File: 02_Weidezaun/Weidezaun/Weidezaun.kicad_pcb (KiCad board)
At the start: 2 copper layers, 34.3 x 47.7 mm, 8 parts, among them J1 Screw_Terminal_01x02, J2 Screw_Terminal_01x02, Q1 2N7000

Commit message: review
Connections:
- J1 pad 2: Net-(BZ1-Pad1) -> +9V
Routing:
- net +9V: track 29.3 -> 69.9 mm
- net Net-(BZ1-Pad1): track 32.9 -> 18.7 mm
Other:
- board text added: "GND"
- board text added: "SPEAKER"
- board text added: "VCC"
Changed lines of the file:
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@@
   (general
     (thickness 1.6)
-    (drawings 4)
-    (tracks 16)
+    (drawings 7)
+    (tracks 20)
     (zones 0)
     (modules 8)
@@
     (47 F.CrtYd user)
     (48 B.Fab user)
-    (49 F.Fab user)
+    (49 F.Fab user hide)
   )
   (setup
@@
     (pad_to_mask_clearance 0)
     (aux_axis_origin 0 0)
-    (visible_elements FFFFFF7F)
+    (visible_elements 7FFFFFFF)
     (pcbplotparams
       (layerselection 0x010fc_ffffffff)
@@
     (descr "simple 2-pin terminal block, pitch 5.08mm, revamped version of bornier2")
     (tags "terminal block bornier2")
-    (fp_text reference J1 (at 2.73 -2.88) (layer F.SilkS)
+    (fp_text reference J1 (at -0.756 -2.9304) (layer F.SilkS)
       (effects (font (size 1 1) (thickness 0.15)))
     )
     (fp_text value Screw_Terminal_01x02 (at 2.54 5.08) (layer F.Fab)
-      (effects (font (size 1 1) (thickness 0.15)))
-    )
-    (fp_text user %R (at 2.54 0) (layer F.Fab)
       (effects (font (size 1 1) (thickness 0.15)))
     )
@@
     (fp_line (start 7.79 4) (end 7.79 -4) (layer F.CrtYd) (width 0.05))
     (fp_line (start 7.79 4) (end -2.71 4) (layer F.CrtYd) (width 0.05))
+    (fp_text user %R (at 2.54 0) (layer F.Fab)
+      (effects (font (size 1 1) (thickness 0.15)))
+    )
     (pad 2 thru_hole circle (at 5.08 0) (size 3 3) (drill 1.52) (layers *.Cu *.Mask)
-      (net 2 "Net-(BZ1-Pad1)"))
+      (net 3 +9V))
     (pad 1 thru_hole rect (at 0 0) (size 3 3) (drill 1.52) (layers *.Cu *.Mask)
       (net 1 "Net-(BZ1-Pad2)"))
@@
   (module custom:testpoint_15x15 (layer F.Cu)
     (at 120.37 101.815001)
-    (fp_text reference TP2 (at 0 -8.265001) (layer F.SilkS)
+    (fp_text reference TP2 (at 5.8934 -6.615801) (layer Dwgs.User)
       (effects (font (size 1 1) (thickness 0.15)))
     )
@@
   (module custom:testpoint_15x15 (layer F.Cu)
     (at 120.37 71.264999)
-    (fp_text reference TP1 (at 0 8.355001) (layer F.SilkS)
+    (fp_text reference TP1 (at 0 8.355001) (layer Dwgs.User)
       (effects (font (size 1 1) (thickness 0.15)))
     )
@@
     (fp_text value 220R (at 3.81 1.92) (layer F.Fab)
       (effects (font (size 1 1) (thickness 0.15)))
-    )
-    (fp_text user %R (at 3.81 0) (layer F.Fab)
-      (effects (font (size 0.72 0.72) (thickness 0.108)))
     )
     (fp_line (start 2.01 -0.8) (end 2.01 0.8) (layer F.Fab) (width 0.1))
@@
     (fp_line (start 8.57 1.05) (end 8.57 -1.05) (layer F.CrtYd) (width 0.05))
     (fp_line (start 8.57 -1.05) (end -0.95 -1.05) (layer F.CrtYd) (width 0.05))
+    (fp_text user %R (at 3.81 0) (layer F.Fab)
+      (effects (font (size 0.72 0.72) (thickness 0.108)))
+    )
     (pad 2 thru_hole oval (at 7.62 0) (size 1.4 1.4) (drill 0.7) (layers *.Cu *.Mask)
       (net 2 "Net-(BZ1-Pad1)"))
@@
     (fp_text value 1M (at 3.81 1.92 90) (layer F.Fab)
       (effects (font (size 1 1) (thickness 0.15)))
-    )
-    (fp_text user %R (at 3.81 0 90) (layer F.Fab)
-      (effects (font (size 0.72 0.72) (thickness 0.108)))
     )
     (fp_line (start 2.01 -0.8) (end 2.01 0.8) (layer F.Fab) (width 0.1))
@@
     (fp_line (start 8.57 1.05) (end 8.57 -1.05) (layer F.CrtYd) (width 0.05))
     (fp_line (start 8.57 -1.05) (end -0.95 -1.05) (layer F.CrtYd) (width 0.05))
+    (fp_text user %R (at 3.81 0 90) (layer F.Fab)
+      (effects (font (size 0.72 0.72) (thickness 0.108)))
+    )
     (pad 2 thru_hole oval (at 7.62 0 90) (size 1.4 1.4) (drill 0.7) (layers *.Cu *.Mask)
       (net 4 GND))
@@
       (effects (font (size 1 1) (thickness 0.15)))
     )
-    (fp_arc (start 1.27 0) (end 1.27 -2.6) (angle 135) (layer F.SilkS) (width 0.12))
-    (fp_arc (start 1.27 0) (end 1.27 -2.48) (angle -135) (layer F.Fab) (width 0.1))
-    (fp_arc (start 1.27 0) (end 1.27 -2.6) (angle -135) (layer F.SilkS) (width 0.12))
-    (fp_arc (start 1.27 0) (end 1.27 -2.48) (angle 135) (layer F.Fab) (width 0.1))
-    (fp_text user %R (at 1.27 0 90) (layer F.Fab)
-      (effects (font (size 1 1) (thickness 0.15)))
-    )
     (fp_line (start -0.53 1.85) (end 3.07 1.85) (layer F.SilkS) (width 0.12))
     (fp_line (start -0.5 1.75) (end 3 1.75) (layer F.Fab) (width 0.1))
@@
     (fp_line (start 4 2.01) (end 4 -2.73) (layer F.CrtYd) (width 0.05))
     (fp_line (start 4 2.01) (end -1.46 2.01) (layer F.CrtYd) (width 0.05))
+    (fp_arc (start 1.27 0) (end 1.27 -2.6) (angle 135) (layer F.SilkS) (width 0.12))
+    (fp_arc (start 1.27 0) (end 1.27 -2.48) (angle -135) (layer F.Fab) (width 0.1))
+    (fp_arc (start 1.27 0) (end 1.27 -2.6) (angle -135) (layer F.SilkS) (width 0.12))
+    (fp_arc (start 1.27 0) (end 1.27 -2.48) (angle 135) (layer F.Fab) (width 0.1))
+    (fp_text user %R (at 1.27 0 90) (layer F.Fab)
+      (effects (font (size 1 1) (thickness 0.15)))
+    )
     (pad 1 thru_hole rect (at 0 0 270) (size 1.05 1.5) (drill 0.75) (layers *.Cu *.Mask)
       (net 4 GND))
@@
     )
     (fp_text value Screw_Terminal_01x02 (at 2.54 5.08) (layer F.Fab)
-      (effects (font (size 1 1) (thickness 0.15)))
-    )
-    (fp_text user %R (at 2.54 0) (layer F.Fab)
       (effects (font (size 1 1) (thickness 0.15)))
     )
@@
     (fp_line (start 7.79 4) (end 7.79 -4) (layer F.CrtYd) (width 0.05))
     (fp_line (start 7.79 4) (end -2.71 4) (layer F.CrtYd) (width 0.05))
+    (fp_text user %R (at 2.54 0) (layer F.Fab)
+      (effects (font (size 1 1) (thickness 0.15)))
+    )
     (pad 2 thru_hole circle (at 5.08 0 180) (size 3 3) (drill 1.52) (layers *.Cu *.Mask)
       (net 3 +9V))
@@
       (effects (font (size 1 1) (thickness 0.15)))
     )
-    (fp_arc (start 2.5 0) (end -3.9 -1.5) (angle -26.38121493) (layer F.SilkS) (width 0.12))
-    (fp_text user %R (at 2.5 -2.43) (layer F.Fab)
-      (effects (font (size 1 1) (thickness 0.15)))
-    )
     (fp_circle (center 2.5 0) (end 8.85 0) (layer F.CrtYd) (width 0.05))
     (fp_circle (center 2.5 0) (end 8.6 0) (layer F.Fab) (width 0.1))
@@
     (fp_circle (center 2.5 0) (end 8.73 0) (layer F.SilkS) (width 0.12))
     (fp_line (start -1.3 -1) (end -1.3 1) (layer F.Fab) (width 0.1))
+    (fp_arc (start 2.5 0) (end -3.9 -1.5) (angle -26.38121493) (layer F.SilkS) (width 0.12))
+    (fp_text user %R (at 2.5 -2.43) (layer F.Fab)
+      (effects (font (size 1 1) (thickness 0.15)))
+    )
     (pad 2 thru_hole circle (at 5 0 180) (size 2 2) (drill 1) (layers *.Cu *.Mask)
       (net 1 "Net-(BZ1-Pad2)"))
@@
       (rotate (xyz 0 0 0))
     )
+  )
+  (gr_text SPEAKER (at 140.7668 101.3714) (layer F.SilkS)
+    (effects (font (size 1.5 1.5) (thickness 0.3)))
+  )
+  (gr_text VCC (at 138.1252 71.6534 180) (layer F.SilkS)
+    (effects (font (size 1.5 1.5) (thickness 0.3)))
+  )
+  (gr_text GND (at 143.2052 71.6788 180) (layer F.SilkS)
+    (effects (font (size 1.5 1.5) (thickness 0.3)))
   )
   (gr_line (start 145.96 110.42) (end 145.96 62.7) (layer Edge.Cuts) (width 0.05))
@@
   (segment (start 136.050785 104.290785) (end 138.17 106.41) (width 0.5) (layer F.Cu) (net 1))
   (segment (start 136.050785 93.06) (end 136.050785 104.290785) (width 0.5) (layer F.Cu) (net 1))
-  (segment (start 143.25 95.259215) (end 141.050785 93.06) (width 0.5) (layer F.Cu) (net 2))
-  (segment (start 143.25 106.41) (end 143.25 95.259215) (width 0.5) (layer F.Cu) (net 2))
   (segment (start 142.49 91.620785) (end 142.49 75) (width 0.5) (layer F.Cu) (net 2))
   (segment (start 141.050785 93.06) (end 142.49 91.620785) (width 0.5) (layer F.Cu) (net 2))
   (segment (start 124.934999 66.7) (end 120.37 71.264999) (width 0.5) (layer F.Cu) (net 3))
   (segment (start 138.16 66.7) (end 124.934999 66.7) (width 0.5) (layer F.Cu) (net 3))
-  (segment (start 138.16 71.71) (end 134.87 75) (width 0.5) (layer F.Cu) (net 3))
   (segment (start 138.16 66.7) (end 138.16 71.71) (width 0.5) (layer F.Cu) (net 3))
+  (segment (start 138.0439 71.8261) (end 134.87 75) (width 0.5) (layer F.Cu) (net 3))
+  (segment (start 138.16 71.71) (end 138.0439 71.8261) (width 0.5) (layer F.Cu) (net 3))
+  (segment (start 142.7175 71.8261) (end 138.0439 71.8261) (width 0.5) (layer F.Cu) (net 3))
+  (segment (start 144.526 73.6346) (end 142.7175 71.8261) (width 0.5) (layer F.Cu) (net 3))
+  (segment (start 144.526 105.2322) (end 144.526 73.6346) (width 0.5) (layer F.Cu) (net 3))
+  (segment (start 143.3482 106.41) (end 144.526 105.2322) (width 0.5) (layer F.Cu) (net 3))
+  (segment (start 143.25 106.41) (end 143.3482 106.41) (width 0.5) (layer F.Cu) (net 3))
   (segment (start 134.97 87.215001) (end 120.37 101.815001) (width 0.5) (layer F.Cu) (net 5))
   (segment (start 134.97 85.38) (end 134.97 87.215001) (width 0.5) (layer F.Cu) (net 5))

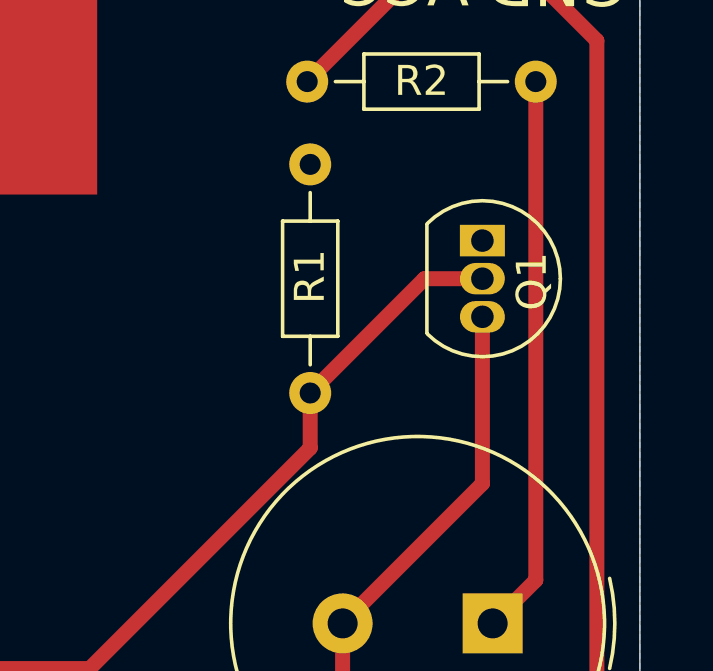
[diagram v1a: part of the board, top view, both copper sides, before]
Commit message: changed footprint
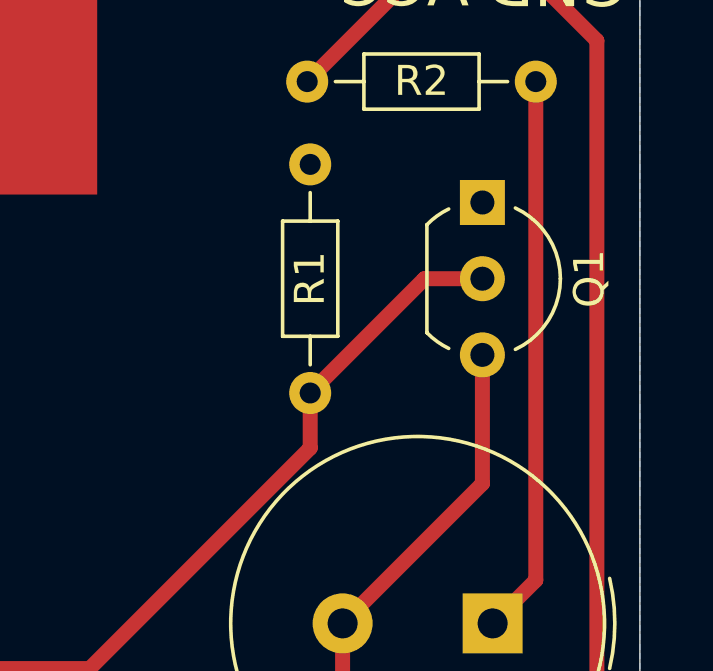
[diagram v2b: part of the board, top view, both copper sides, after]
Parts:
- Q1: footprint Package_TO_SOT_THT:TO-92_Inline -> Package_TO_SOT_THT:TO-92_Inline_Wide
- moved Q1 1.27 mm to (140.7, 79.0)
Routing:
- net Net-(BZ1-Pad2): track 26.4 -> 25.1 mm
